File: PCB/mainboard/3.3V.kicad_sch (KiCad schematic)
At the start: 8 parts, among them U2 TPS5430DDA

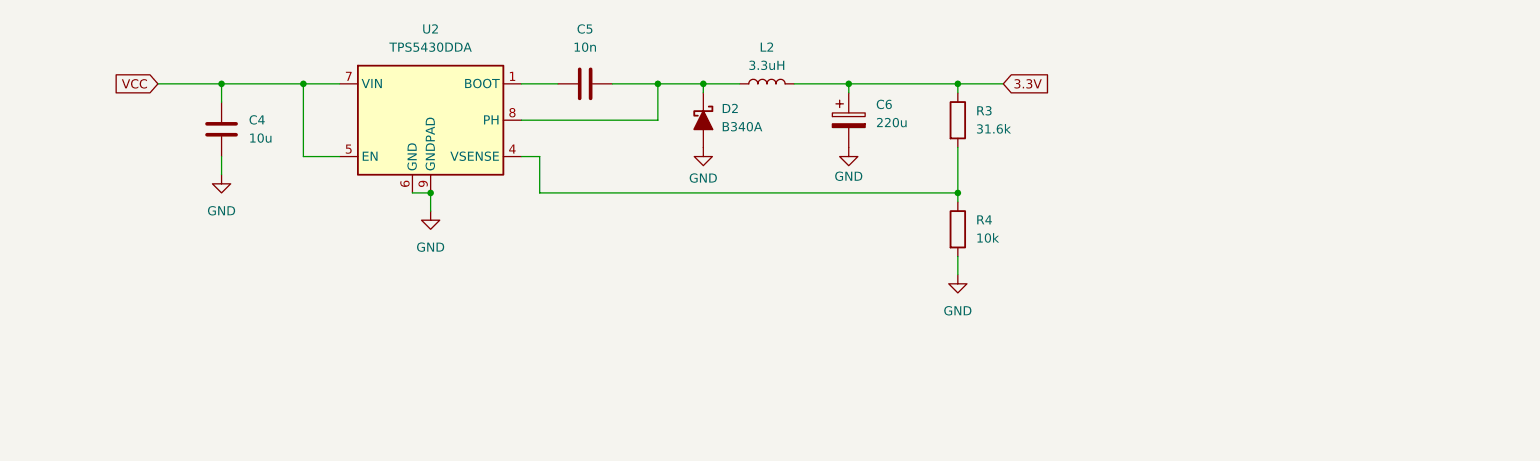
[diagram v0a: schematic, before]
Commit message: upgrades to STM32 Board
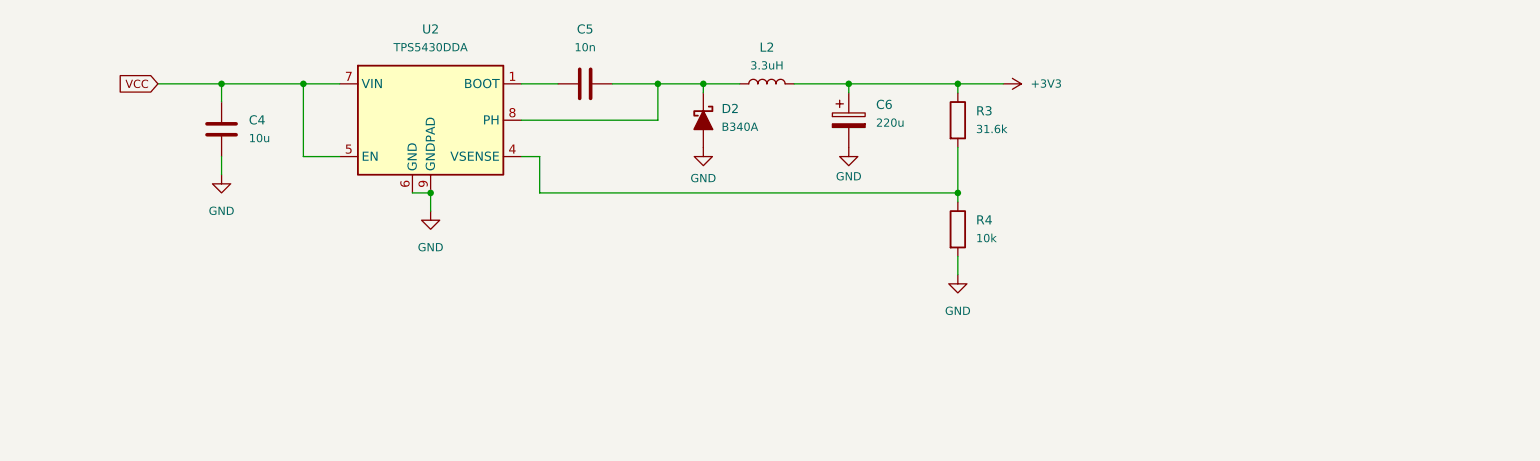
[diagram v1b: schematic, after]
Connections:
- net 3.3V renamed +3V3
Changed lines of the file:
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@@
 		(effects
 			(font
-				(size 1.27 1.27)
+				(size 1.143 1.143)
 			)
 			(justify right)
@@
 		)
 	)
-	(global_label "3.3V"
-		(shape input)
-		(at 194.31 71.12 0)
-		(fields_autoplaced yes)
-		(effects
-			(font
-				(size 1.27 1.27)
-			)
-			(justify left)
-		)
-		(property "Intersheetrefs" "${INTERSHEET_REFS}"
-			(at 201.4076 71.12 0)
-			(effects
-				(font
-					(size 1.27 1.27)
-				)
-				(justify left)
-				(hide yes)
-			)
-		)
-	)
 	(symbol
 		(lib_id "power:GND")
@@
 			(effects
 				(font
-					(size 1.27 1.27)
+					(size 1.143 1.143)
 				)
 			)
@@
 			(effects
 				(font
-					(size 1.27 1.27)
+					(size 1.143 1.143)
 				)
 			)
@@
 			(effects
 				(font
-					(size 1.27 1.27)
+					(size 1.143 1.143)
 				)
 			)
@@
 			(effects
 				(font
-					(size 1.27 1.27)
+					(size 1.143 1.143)
 				)
 			)
@@
 			(effects
 				(font
-					(size 1.27 1.27)
+					(size 1.143 1.143)
 				)
 				(justify left)
@@
 			(effects
 				(font
-					(size 1.27 1.27)
+					(size 1.143 1.143)
 				)
 			)
@@
 			(effects
 				(font
-					(size 1.27 1.27)
+					(size 1.143 1.143)
 				)
 			)
@@
 			(effects
 				(font
-					(size 1.27 1.27)
+					(size 1.143 1.143)
 				)
 				(justify right)
@@
 			(effects
 				(font
-					(size 1.27 1.27)
+					(size 1.143 1.143)
 				)
 			)
@@
 			(effects
 				(font
-					(size 1.27 1.27)
+					(size 1.143 1.143)
 				)
 				(justify left)
@@
 			(effects
 				(font
-					(size 1.27 1.27)
+					(size 1.143 1.143)
 				)
 				(justify left)
@@
 	)
 	(symbol
+		(lib_id "power:+3V3")
+		(at 194.31 71.12 270)
+		(unit 1)
+		(exclude_from_sim no)
+		(in_bom yes)
+		(on_board yes)
+		(dnp no)
+		(fields_autoplaced yes)
+		(property "Reference" "#PWR0103"
+			(at 190.5 71.12 0)
+			(effects
+				(font
+					(size 1.27 1.27)
+				)
+				(hide yes)
+			)
+		)
+		(property "Value" "+3V3"
+			(at 198.12 71.1199 90)
+			(effects
+				(font
+					(size 1.143 1.143)
+				)
+				(justify left)
+			)
+		)
+		(property "Footprint" ""
+			(at 194.31 71.12 0)
+			(effects
+				(font
+					(size 1.27 1.27)
+				)
+				(hide yes)
+			)
+		)
+		(property "Datasheet" ""
+			(at 194.31 71.12 0)
+			(effects
+				(font
+					(size 1.27 1.27)
+				)
+				(hide yes)
+			)
+		)
+		(property "Description" "Power symbol creates a global label with name \"+3V3\""
+			(at 194.31 71.12 0)
+			(effects
+				(font
+					(size 1.27 1.27)
+				)
+				(hide yes)
+			)
+		)
+		(pin "1"
+		)
+		(instances
+			(project ""
+				(path "/d49cf26c-5888-451d-a9f9-a714323b15a2/a8b3cc2d-7554-40f3-826c-dc6c2c398d19"
+					(reference "#PWR0103")
+					(unit 1)
+				)
+			)
+		)
+	)
+	(symbol
 		(lib_id "power:GND")
 		(at 114.3 88.9 0)
@@
 			(effects
 				(font
-					(size 1.27 1.27)
+					(size 1.143 1.143)
 				)
 			)
@@
 			(effects
 				(font
-					(size 1.27 1.27)
+					(size 1.143 1.143)
 				)
 				(justify left)

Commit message: Made the Mainboard BCP Part Layout
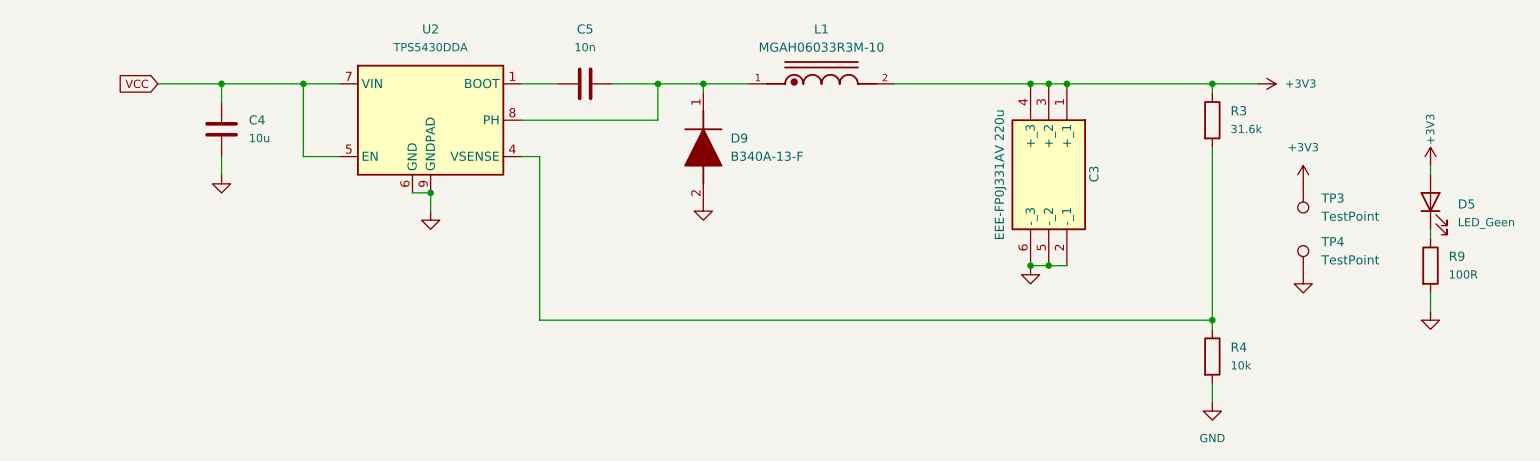
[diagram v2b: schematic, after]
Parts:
- removed C6: 220u, lib:EEEFP0J331AV, symbol Device:C_Polarized
- removed D2: B340A, PCM_Diode_SMD_AKL:D_SMA, symbol PCM_Diode_Schottky_AKL:B340A
- removed L2: 3.3uH, lib:IND_MGAH06033R3M-10, symbol Device:L
- added C3: EEE-FP0J331AV 220u, lib:EEEFP0J331AV, symbol EEE-FP0J331AV:EEE-FP0J331AV
- added D5: LED_Geen, lib:LEDC1608X70N, symbol Device:LED
- added D9: B340A-13-F, lib:DIOM5226X240N, symbol B340A-13-F:B340A-13-F
- added L1: MGAH06033R3M-10, lib:IND_MGAH06033R3M-10, symbol MGAH06033R3M-10:MGAH06033R3M-10
- added R9: 100R, Resistor_SMD:R_0201_0603Metric_Pad0.64x0.40mm_HandSolder, symbol Device:R
- added TP3, TP4: TestPoint, TestPoint:TestPoint_Pad_D2.0mm, symbol Connector:TestPoint
- R3, R4: footprint Resistor_SMD:R_0201_0603Metric_Pad0.64x0.40mm_HandSolder -> Resistor_SMD:R_0402_1005Metric_Pad0.72x0.64mm_HandSolder
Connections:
- net +3V3: now also C3.1 (+_1), C3.3 (+_2), C3.4 (+_3), D5.2 (A), L1.2, TP3.1
- net GND: now also C3.2 (-_1), C3.5 (-_2), C3.6 (-_3), D9.2 (A), R9.2, TP4.1
- net at C5.2, U2.8 (PH): now also D9.1 (K), L1.1
- new net: D5.1 (K), R9.1
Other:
- moved on the sheet: R3, R4

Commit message: Stop tracking renders folder & final Powerstrip and Mainboard PCB
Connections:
- net PH 3.3: now reaches C5.2, D9.1 (K), L1.1, U2.8 (PH)
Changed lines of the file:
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@@
+		)
+	)
+	(global_label "PH 3.3"
+		(shape input)
+		(at 146.05 71.12 90)
+		(fields_autoplaced yes)
+		(effects
+			(font
+				(size 1.143 1.143)
+			)
+			(justify left)
+		)
+		(property "Intersheetrefs" "${INTERSHEET_REFS}"
+			(at 146.05 62.5007 90)
+			(effects
+				(font
+					(size 1.27 1.27)
+				)
+				(justify left)
+				(hide yes)
+			)
 		)
 	)

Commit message: random upload
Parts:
- removed C3: EEE-FP0J331AV 220u, lib:EEEFP0J331AV, symbol EEE-FP0J331AV:EEE-FP0J331AV
- removed D9: B340A-13-F, lib:DIOM5226X240N, symbol B340A-13-F:B340A-13-F
- removed L1: MGAH06033R3M-10, lib:IND_MGAH06033R3M-10, symbol MGAH06033R3M-10:MGAH06033R3M-10
- removed U2: TPS5430DDA, Package_SO:TI_SO-PowerPAD-8_ThermalVias, symbol Regulator_Switching:TPS5430DDA
- added C1: 10u, Capacitor_SMD:C_0402_1005Metric_Pad0.74x0.62mm_HandSolder, symbol Device:C
- added C2: 100n, Capacitor_SMD:C_0402_1005Metric_Pad0.74x0.62mm_HandSolder, symbol Device:C
- added C3: 10n, Capacitor_SMD:C_0402_1005Metric_Pad0.74x0.62mm_HandSolder, symbol Device:C
- added R1: 27.4k, Resistor_SMD:R_0402_1005Metric_Pad0.72x0.64mm_HandSolder, symbol Device:R
- added R2: 10k, Resistor_SMD:R_0402_1005Metric_Pad0.72x0.64mm_HandSolder, symbol Device:R
- added VR2: TPSM863252RDXR, lib:VREG_TPSM863252RDXR, symbol TPSM863252RDXR:TPSM863252RDXR
- C4: value 10u -> 22p; footprint Capacitor_SMD:C_1206_3216Metric_Pad1.33x1.80mm_HandSolder -> Capacitor_SMD:C_0402_1005Metric_Pad0.74x0.62mm_HandSolder
- C5: value 10n -> 33u; footprint Capacitor_SMD:C_1206_3216Metric_Pad1.33x1.80mm_HandSolder -> lib:C4532_Commercial
- R3: value 31.6k -> 220k
- R4: value 10k -> 30k
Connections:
- net PH 3.3 is gone; now on net GND: C5.2
- net +3V3: now also C4.1, C5.1, VR2.3 (VOUT)
- net GND: now also C1.2, C2.2, C3.2, R2.2, VR2.4 (PGND); no longer C4.2
- net VCC: now also C1.1, C2.1, R1.1, VR2.1 (VIN); no longer C4.1
- net at R3.2, R4.1: now also C4.2, VR2.7 (FB)
- new net: C3.1, R1.2, R2.1, VR2.6 (EN)
- no-connect marks 0 -> 1
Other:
- note added: "5.8V-8.4V to 5.0V @ 2A"
- moved on the sheet: D5, R9, TP3, TP4
